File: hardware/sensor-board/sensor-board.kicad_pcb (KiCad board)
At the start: 2 copper layers, 65 x 88 mm, 81 parts, among them J1 HELM, J2 TACH, J4 RPi GPIO, J5 NMEA 2000, J6 LIGHTS, J7 5V IN, Q1 IRLML0030, U1 ADS1115IDGSR, U2 ADS1115IDGSR, U3 EL817, U4 MCP2518FD, U5 ISO1044BD, U6 UA78L05, U7 LM74700-Q1, Y1 40MHz

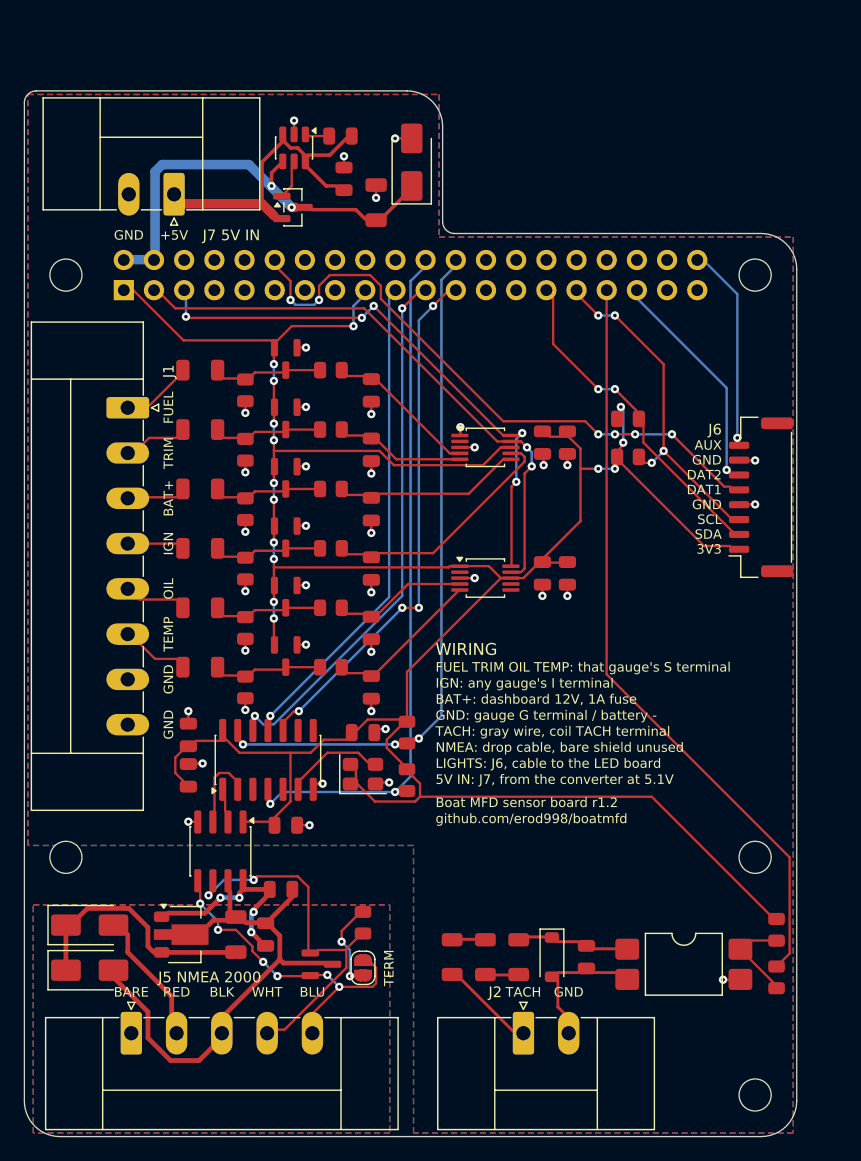
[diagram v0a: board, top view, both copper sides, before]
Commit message: Sensor board rev 1.3 built and checked, with a house battery input; the dashboard reads it
The boat has two batteries on a common negative, positives kept apart (house: lights and
stereo). J1.8, a second GND until now, becomes HSE+: the house battery through the same
47k/10k divider, BAT54S clamp and 1k/100n filter as the engine battery (J1.3, now labelled
ENG+), into U2 AIN2 (software channel 6). Its parts (R35-R37, D13, C24) take the next free
numbers; with no room left in the input column, its lane runs right to left beside U2.
design.channel_refs/channel_sch give each channel its parts and its place on the schematic.

Rev 1.3 (the cloud session's RJ45 link) is now built under KiCad and passes ERC, DRC and
parity with nothing reported; fab/ is regenerated from it. Fixes on the way: the RJ45's two
labels moved off the link's resistors and the board edge into the strip left of the jack
("J6 LED LINK", "NOT ETHERNET"); C22's GND pad, boxed in with room for one thermal spoke,
joins GND by its own via rather than the top pour; the legend moves down 1 mm for the new lane.

Dashboard: BOAT_HOUSE_BATTERY=true reads it (in tap and n2k modes). The BATTERY tile shows
"HOUSE 13.2 V" under its label, level with the engine battery's number (fits at 1180, 1280
and 1920 wide); house low/high alarms in the battery tile's menu, shown only where there is a
house reading, without painting the engine battery's bar; its own calibration on /calibrate;
a "House battery" data box; the simulator has a house battery charged while the engine runs.

Co-Authored-By: Claude Opus 5.5 <noreply@anthropic.com>
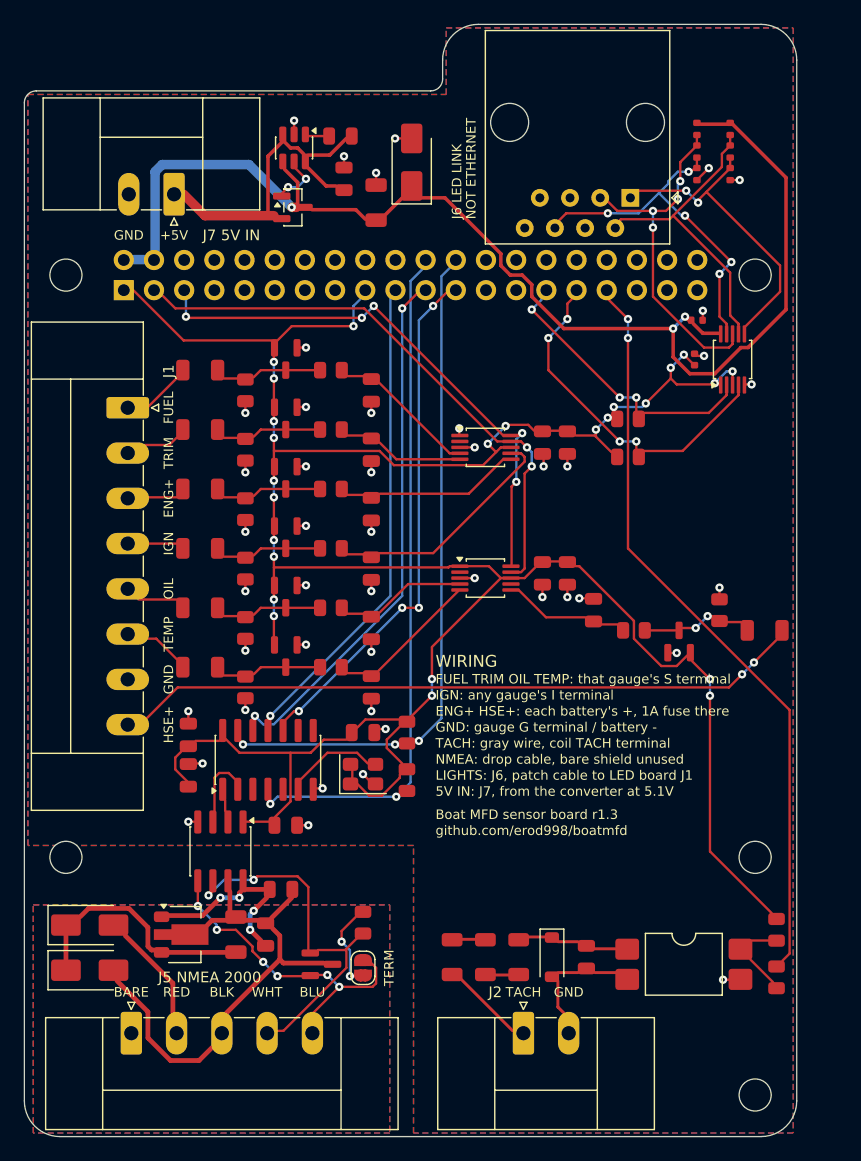
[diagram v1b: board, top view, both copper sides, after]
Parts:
- added C22: 100n, sensor-board:C_0402_1005Metric_NoSilk, F.Cu at (156.4, 60.6)
- added C23: 100n, sensor-board:C_0402_1005Metric_NoSilk, F.Cu at (156.6, 57.3)
- added C24: 100n, sensor-board:C_0805_2012Metric_NoSilk, F.Cu at (147.9, 81.7)
- added D13: BAT54S, sensor-board:SOT-23_NoSilk, F.Cu at (155.1, 84.3)
- added R29: 620, sensor-board:R_0402_1005Metric_NoSilk, F.Cu at (159.4, 41.2)
- added R30: 120, sensor-board:R_0402_1005Metric_NoSilk, F.Cu at (159.4, 43.1)
- added R31: 620, sensor-board:R_0402_1005Metric_NoSilk, F.Cu at (159.4, 45.0)
- added R32: 620, sensor-board:R_0402_1005Metric_NoSilk, F.Cu at (156.6, 41.2)
- added R33: 120, sensor-board:R_0402_1005Metric_NoSilk, F.Cu at (156.6, 43.1)
- added R34: 620, sensor-board:R_0402_1005Metric_NoSilk, F.Cu at (156.6, 45.0)
- added R35: 47k, sensor-board:R_1206_3216Metric_NoSilk, F.Cu at (162.3, 83.4)
- added R36: 10k, sensor-board:R_0805_2012Metric_NoSilk, F.Cu at (158.5, 81.7)
- added R37: 1k, sensor-board:R_0805_2012Metric_NoSilk, F.Cu at (151.3, 83.4)
- added U8: PCA9615DP, Package_SO:TSSOP-10_3x3mm_P0.5mm, F.Cu at (159.6, 60.6)
- J6: footprint Connector_JST:JST_GH_SM08B-GHS-TB_1x08-1MP_P1.25mm_Horizontal -> Connector_RJ:RJ45_Amphenol_54602-x08_Horizontal
- moved J6 27.5 mm to (151.0, 47.0), turned to 180 degrees
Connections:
- J1 pad 8: GND -> /HOUSE_IN
- J4 pad 12: /LIGHT_DAT1 -> unconnected-(J4-Pin_12-Pad12)
- J4 pad 35: /LIGHT_DAT2 -> unconnected-(J4-Pin_35-Pad35)
- J4 pad 40: /LIGHT_AUX -> unconnected-(J4-Pin_40-Pad40)
- J6 pad 1: +3V3 -> /LINK_SCLM
- J6 pad 2: /LIGHT_SDA -> /LINK_SCLP
- J6 pad 3: /LIGHT_SCL -> /LINK_SDAP
- J6 pad 4: GND -> unconnected-(J6-Pad4)
- J6 pad 5: /LIGHT_DAT1 -> unconnected-(J6-Pad5)
- J6 pad 6: /LIGHT_DAT2 -> /LINK_SDAM
- J6 pad 7: GND -> unconnected-(J6-Pad7)
- J6 pad 8: /LIGHT_AUX -> unconnected-(J6-Pad8)
- U2 pad 6: unconnected-(U2-AIN2-Pad6) -> /HOUSE_ADC
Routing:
- net +5V: track 30.0 -> 97.4 mm, vias 2 -> 3
- net /HOUSE_IN: track 0.00 -> 55.7 mm, vias 0 -> 2
- net /LIGHT_DAT1: track 49.9 -> 0.00 mm, vias 6 -> 0
- net /LINK_SDAM: track 0.00 -> 28.3 mm, vias 0 -> 5
- net /LINK_SDAP: track 0.00 -> 28.0 mm, vias 0 -> 4
- net /LINK_SCLM: track 0.00 -> 24.7 mm, vias 0 -> 2
- net /LINK_SCLP: track 0.00 -> 24.3 mm
- net /LIGHT_DAT2: track 17.7 -> 0.00 mm, vias 1 -> 0
- net /LIGHT_AUX: track 16.2 -> 0.00 mm, vias 1 -> 0
- net /HOUSE_ADC: track 0.00 -> 7.85 mm
- net /HOUSE_DIV: track 0.00 -> 6.31 mm, vias 0 -> 2
- net +3V3: track 205.7 -> 202.1 mm, vias 15 -> 25
- net GND: track 20.8 -> 24.3 mm, vias 39 -> 45
- net /LIGHT_SDA: track 25.2 -> 22.0 mm, vias 2 -> 3
- net /IDEAL_G: track 2.35 -> 3.77 mm, vias 0 -> 2
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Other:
- board size 65 x 88 mm -> 65 x 93.6 mm
- board text added: "Boat MFD sensor board r1.3"
- board text added: "ENG+"
- board text added: "ENG+ HSE+: each battery's +, 1A fuse there"
- board text added: "HSE+"
- board text added: "J6 LED LINK"
- board text added: "LIGHTS: J6, patch cable to LED board J1"
- board text added: "NOT ETHERNET"
- board text removed: "3V3"
- board text removed: "AUX"
- board text removed: "BAT+"
- board text removed: "BAT+: dashboard 12V, 1A fuse"
- board text removed: "Boat MFD sensor board r1.2"
- board text removed: "DAT1"
- board text removed: "DAT2"
- board text removed: "J6"
- board text removed: "LIGHTS: J6, cable to the LED board"
- board text removed: "SCL"
- board text removed: "SDA"
